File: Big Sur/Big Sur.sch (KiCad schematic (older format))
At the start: 0 parts

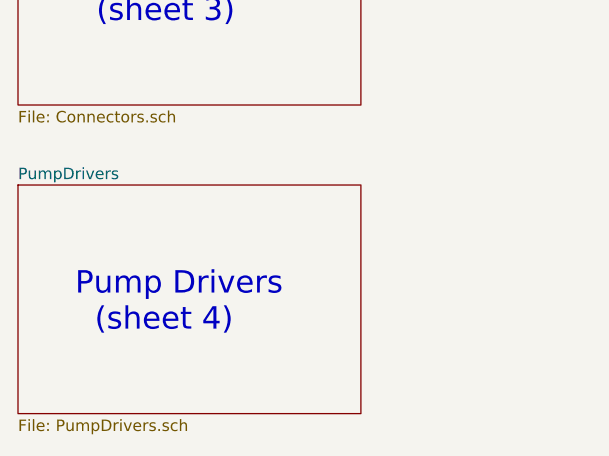
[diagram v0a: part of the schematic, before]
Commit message: Updated current sense, second pump driver, solenoid connectors
-Current sense now uses current sense ICs, connected to Paraduino ADC pins.
-Added second pump driver.
-Connected outputs with XT30 connectors.
-Still need some Paraduino connections, inverter driver, footprints.
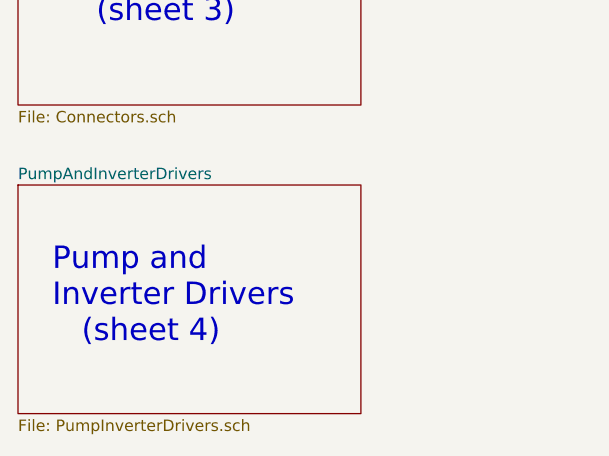
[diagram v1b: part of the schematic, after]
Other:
- note added: "Pump and\nInverter Drivers\n (sheet 4)"
- note removed: "Pump Drivers\n (sheet 4)"
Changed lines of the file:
@@
 S 1950 4100 1500 1000
 U 5D7D29A6
-F0 "PumpDrivers" 50
-F1 "PumpDrivers.sch" 50
+F0 "PumpAndInverterDrivers" 50
+F1 "PumpInverterDrivers.sch" 50
 $EndSheet
-Text Notes 2200 4750 0    98   ~ 0
-Pump Drivers\n  (sheet 4)
+Text Notes 2100 4800 0    98   ~ 0
+   Pump and\nInverter Drivers\n   (sheet 4)
 Text Notes 2100 2100 0    98   ~ 0
 Solenoid Drivers\n   (sheet 2)

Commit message: Removed Inverter
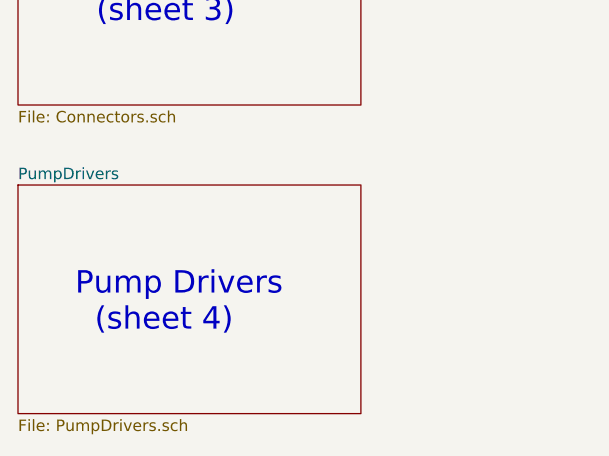
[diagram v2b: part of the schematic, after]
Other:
- note added: "Pump Drivers\n (sheet 4)"
- note removed: "Pump and\nInverter Drivers\n (sheet 4)"
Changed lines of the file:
@@
 Comp "Paradigm Hyperloop"
 Comment1 ""
-Comment2 ""
-Comment3 ""
+Comment2 "x"
+Comment3 "x"
 Comment4 "Jasper Rubin"
 $EndDescr
@@
 S 1950 4100 1500 1000
 U 5D7D29A6
-F0 "PumpAndInverterDrivers" 50
-F1 "PumpInverterDrivers.sch" 50
+F0 "PumpDrivers" 50
+F1 "PumpDrivers.sch" 50
 $EndSheet
-Text Notes 2100 4800 0    98   ~ 0
-   Pump and\nInverter Drivers\n   (sheet 4)
+Text Notes 2200 4750 0    98   ~ 0
+Pump Drivers\n  (sheet 4)
 Text Notes 2100 2100 0    98   ~ 0
 Solenoid Drivers\n   (sheet 2)
